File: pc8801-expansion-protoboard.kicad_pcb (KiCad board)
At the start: 2 copper layers, 219 x 95 mm, 4 parts, among them J1 Solder Side, J2 Parts Side

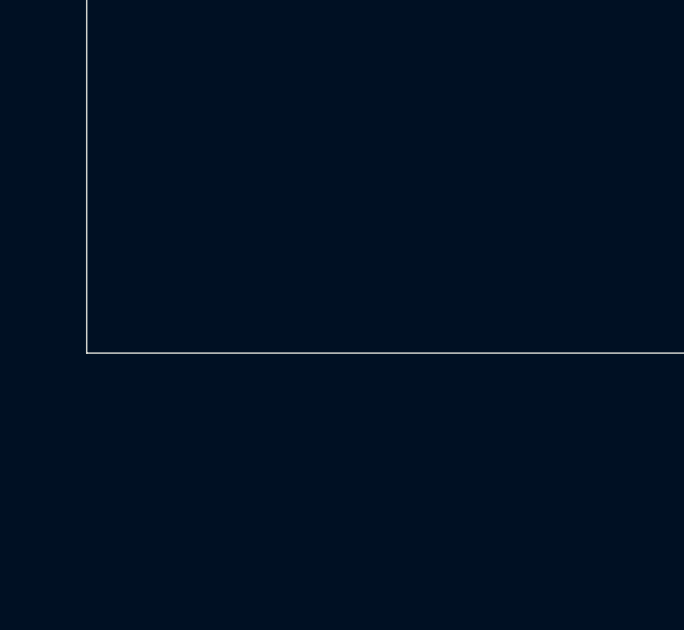
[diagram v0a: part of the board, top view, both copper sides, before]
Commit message: Minor silk prep
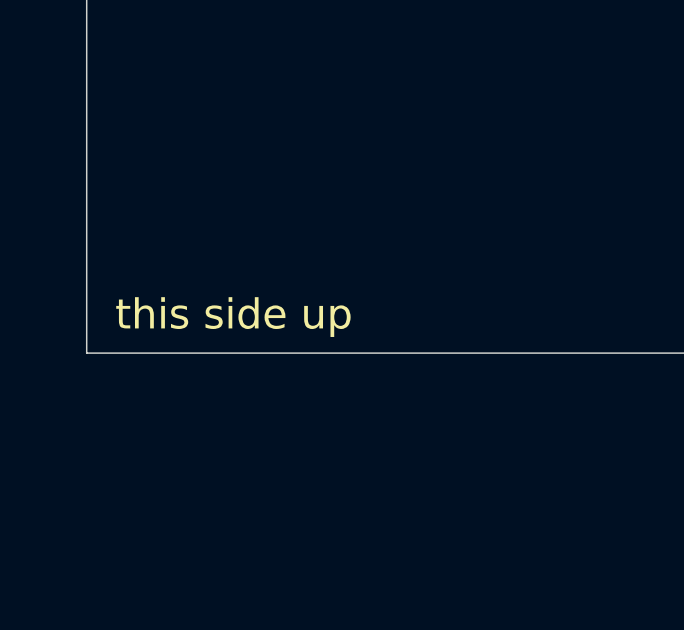
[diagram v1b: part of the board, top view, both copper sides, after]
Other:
- board text added: "this side up"
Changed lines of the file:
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@@
   (general
     (thickness 1.6)
-    (drawings 55)
+    (drawings 57)
     (tracks 7)
     (zones 0)
@@
   )
   (setup
-    (last_trace_width 2)
+    (last_trace_width 0.25)
     (user_trace_width 1)
     (user_trace_width 2)
@@
     (pad 1 np_thru_hole circle (at 0 0) (size 4.3 4.3) (drill 4.3) (layers *.Cu *.Mask))
   )
+  (gr_text "this side up" (at 41.91 132.715) (layer F.SilkS)
+    (effects (font (size 1 1) (thickness 0.15)))
+  )
+  (dimension 219 (width 0.12) (layer F.SilkS)
+    (gr_text "219.000 mm" (at 146.5 21.59) (layer F.SilkS)
+      (effects (font (size 1 1) (thickness 0.15)))
+    )
+    (feature1 (pts (xy 37 50) (xy 37 22.273579)))
+    (feature2 (pts (xy 256 50) (xy 256 22.273579)))
+    (crossbar (pts (xy 256 22.86) (xy 37 22.86)))
+    (arrow1a (pts (xy 37 22.86) (xy 38.126504 22.273579)))
+    (arrow1b (pts (xy 37 22.86) (xy 38.126504 23.446421)))
+    (arrow2a (pts (xy 256 22.86) (xy 254.873496 22.273579)))
+    (arrow2b (pts (xy 256 22.86) (xy 254.873496 23.446421)))
+  )
   (gr_text "AB\n0" (at 116.84 132.08) (layer F.SilkS)

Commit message: Power bars
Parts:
- added J3: 5V, PC-8801:1x20_PowerBar, F.Cu at (45.7, 66.0)
- added J4: 12V, PC-8801:1x20_PowerBar, F.Cu at (237.3, 66.0)
- added J5: -12V, PC-8801:1x20_PowerBar, F.Cu at (241.0, 66.0)
- added J6: GND_1, PC-8801:1x20_PowerBar, F.Cu at (49.5, 66.0)
- added J7: GND_2, PC-8801:1x20_PowerBar, F.Cu at (245.1, 66.0)
- added REF**: 70x20_ProtoArea, PC-8801:70x20_ProtoArea, F.Cu at (143.5, 90.2)
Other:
- board text added: "20 high"
- board text added: "70 wide"

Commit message: Power rails, of a sort
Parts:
- moved J3 3.81 mm to (49.5, 66.0)
- moved J6 3.81 mm to (45.7, 66.0)
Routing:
- net /GND: track 12.7 -> 386.8 mm
- net /+5V: track 15.2 -> 133.7 mm
- net /-12V: track 0.00 -> 103.7 mm
- net /+12V: track 0.00 -> 102.9 mm
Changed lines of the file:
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@@
     (thickness 1.6)
     (drawings 60)
-    (tracks 7)
+    (tracks 34)
     (zones 0)
     (modules 10)
@@
   )
   (setup
-    (last_trace_width 0.25)
+    (last_trace_width 2)
     (user_trace_width 1)
     (user_trace_width 2)
@@
   )
   (module PC-8801:1x20_PowerBar (layer F.Cu)
-    (at 49.53 66.04)
+    (at 45.72 66.04)
     (fp_text reference J6 (at 0 -2.54) (layer F.SilkS) hide
       (effects (font (size 1 1) (thickness 0.15)))
@@
   )
   (module PC-8801:1x20_PowerBar (layer F.Cu)
-    (at 45.72 66.04)
+    (at 49.53 66.04)
     (fp_text reference J3 (at 0 -2.54) (layer F.SilkS) hide
       (effects (font (size 1 1) (thickness 0.15)))
@@
   (segment (start 114.3 129.54) (end 114.3 124.46) (width 2) (layer F.Cu) (net 33))
   (segment (start 114.3 124.46) (end 111.76 124.46) (width 2) (layer F.Cu) (net 33))
+  (segment (start 111.76 124.46) (end 111.76 120.65) (width 2) (layer F.Cu) (net 33))
+  (segment (start 111.76 120.65) (end 110.49 119.38) (width 2) (layer F.Cu) (net 33))
+  (segment (start 110.49 119.38) (end 52.07 119.38) (width 2) (layer F.Cu) (net 33))
+  (segment (start 49.53 116.84) (end 49.53 66.04) (width 2) (layer F.Cu) (net 33))
+  (segment (start 52.07 119.38) (end 49.53 116.84) (width 2) (layer F.Cu) (net 33))
   (segment (start 109.22 124.46) (end 106.68 124.46) (width 2) (layer F.Cu) (net 34))
   (segment (start 106.68 124.46) (end 106.68 129.54) (width 2) (layer F.Cu) (net 34))
   (segment (start 109.22 129.54) (end 109.22 124.46) (width 2) (layer F.Cu) (net 34))
+  (segment (start 53.34 124.46) (end 109.22 124.46) (width 2) (layer F.Cu) (net 34))
+  (segment (start 45.72 116.84) (end 53.34 124.46) (width 2) (layer F.Cu) (net 34))
+  (segment (start 45.72 66.04) (end 45.72 116.84) (width 2) (layer F.Cu) (net 34))
+  (segment (start 45.72 66.04) (end 45.72 63.5) (width 2) (layer F.Cu) (net 34))
+  (segment (start 45.72 63.5) (end 49.53 59.69) (width 2) (layer F.Cu) (net 34))
+  (segment (start 49.53 59.69) (end 242.57 59.69) (width 2) (layer F.Cu) (net 34))
+  (segment (start 245.11 62.23) (end 245.11 114.3) (width 2) (layer F.Cu) (net 34))
+  (segment (start 242.57 59.69) (end 245.11 62.23) (width 2) (layer F.Cu) (net 34))
+  (segment (start 241 66.04) (end 241 114.3) (width 2) (layer F.Cu) (net 37))
+  (segment (start 234.441274 120.310008) (end 234.019992 120.310008) (width 2) (layer F.Cu) (net 37))
+  (segment (start 240.451283 114.3) (end 234.441274 120.310008) (width 2) (layer F.Cu) (net 37))
+  (segment (start 241 114.3) (end 240.451283 114.3) (width 2) (layer F.Cu) (net 37))
+  (segment (start 234.019992 120.310008) (end 233.68 120.65) (width 2) (layer F.Cu) (net 37))
+  (segment (start 233.68 120.65) (end 193.04 120.65) (width 2) (layer F.Cu) (net 37))
+  (segment (start 190.5 123.19) (end 190.5 124.46) (width 2) (layer F.Cu) (net 37))
+  (segment (start 193.04 120.65) (end 190.5 123.19) (width 2) (layer F.Cu) (net 37))
+  (segment (start 237.34 114.3) (end 237.34 66.04) (width 2) (layer F.Cu) (net 38))
+  (segment (start 236.578001 115.061999) (end 237.34 114.3) (width 2) (layer F.Cu) (net 38))
+  (segment (start 192.468715 118.11) (end 233.53 118.11) (width 2) (layer F.Cu) (net 38))
+  (segment (start 187.96 122.618715) (end 192.468715 118.11) (width 2) (layer F.Cu) (net 38))
+  (segment (start 187.96 124.46) (end 187.96 122.618715) (width 2) (layer F.Cu) (net 38))
+  (segment (start 233.53 118.11) (end 236.578001 115.061999) (width 2) (layer F.Cu) (net 38))
   (zone (net 34) (net_name /GND) (layer F.Cu) (hatch edge 0.508)
     (connect_pads yes (clearance 0.508))

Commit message: Here goes nothing
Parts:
- added U1: ExpansionEdge, PC-8801:PC88 Edge, F.Cu at (106.9, 138.7)
- moved J1 2.79 mm to (106.7, 126.7)
- moved J2 2.54 mm to (106.7, 121.9)
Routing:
- net /-12V: track 103.7 -> 166.3 mm
- net /+12V: track 102.9 -> 164.8 mm
- net /GND: track 386.8 -> 433.8 mm, vias 0 -> 4
- net /+5V: track 133.7 -> 177.4 mm, vias 0 -> 4
- net Net-(J2-Pad13): track 0.00 -> 18.0 mm
- net Net-(J2-Pad31): track 0.00 -> 17.8 mm
- net Net-(J2-Pad22): track 0.00 -> 17.8 mm
- net Net-(J2-Pad20): track 0.00 -> 17.8 mm
- net Net-(J2-Pad19): track 0.00 -> 17.8 mm
- net Net-(J2-Pad12): track 0.00 -> 17.8 mm
- net Net-(J2-Pad5): track 0.00 -> 17.8 mm
- net Net-(J2-Pad36): track 0.00 -> 17.8 mm, vias 0 -> 1
- net Net-(J2-Pad30): track 0.00 -> 17.8 mm
- net Net-(J2-Pad29): track 0.00 -> 17.8 mm
- net Net-(J2-Pad27): track 0.00 -> 17.8 mm
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- removed copper zone on F.Cu, net /+5V
- removed copper zone on F.Cu, net /GND

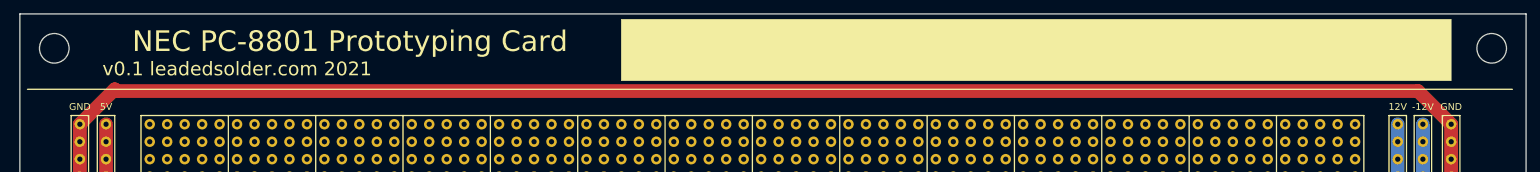
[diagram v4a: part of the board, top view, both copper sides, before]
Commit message: need to fix edge cut
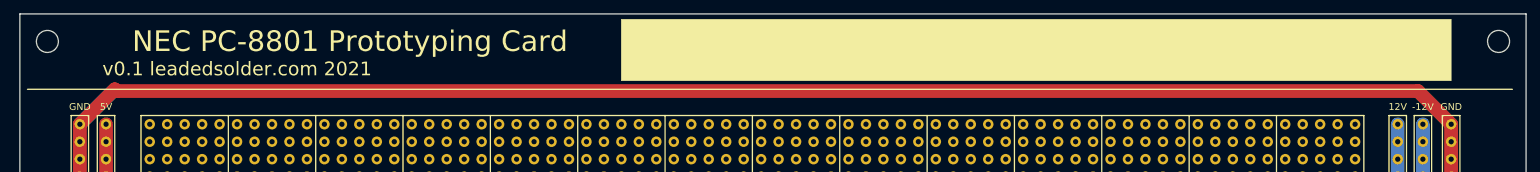
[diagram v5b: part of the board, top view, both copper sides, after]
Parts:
- removed the REF** at (42.0, 55.0)
- removed the REF** at (251.0, 55.0)
- added REF**: MountingHole_3.2mm_M3, MountingHole:MountingHole_3.2mm_M3, F.Cu at (41.0, 54.0)
- added REF**: MountingHole_3.2mm_M3, MountingHole:MountingHole_3.2mm_M3, F.Cu at (252.0, 54.0)
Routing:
- net /GND: track 433.8 -> 440.7 mm
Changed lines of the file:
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@@
   (general
     (thickness 1.6)
-    (drawings 60)
-    (tracks 295)
+    (drawings 64)
+    (tracks 296)
     (zones 0)
     (modules 11)
@@
   )
   (setup
-    (last_trace_width 0.25)
+    (last_trace_width 2)
     (user_trace_width 0.5)
     (user_trace_width 1)
@@
     (add_net "Net-(J2-Pad8)")
     (add_net "Net-(J2-Pad9)")
+  )
+  (module MountingHole:MountingHole_3.2mm_M3 locked (layer F.Cu)
+    (at 41 54)
+    (descr "Mounting Hole 3.2mm, no annular, M3")
+    (tags "mounting hole 3.2mm no annular m3")
+    (attr virtual)
+    (fp_text reference REF** (at 0 -4.2) (layer F.SilkS) hide
+      (effects (font (size 1 1) (thickness 0.15)))
+    )
+    (fp_text value MountingHole_3.2mm_M3 (at 0 4.2) (layer F.Fab)
+      (effects (font (size 1 1) (thickness 0.15)))
+    )
+    (fp_circle (center 0 0) (end 3.45 0) (layer F.CrtYd) (width 0.05))
+    (fp_circle (center 0 0) (end 3.2 0) (layer Cmts.User) (width 0.15))
+    (fp_text user %R (at 0.3 0) (layer F.Fab)
+      (effects (font (size 1 1) (thickness 0.15)))
+    )
+    (pad 1 np_thru_hole circle (at 0 0) (size 3.2 3.2) (drill 3.2) (layers *.Cu *.Mask))
+  )
+  (module MountingHole:MountingHole_3.2mm_M3 locked (layer F.Cu)
+    (at 252 54)
+    (descr "Mounting Hole 3.2mm, no annular, M3")
+    (tags "mounting hole 3.2mm no annular m3")
+    (attr virtual)
+    (fp_text reference REF** (at 0 -4.2) (layer F.SilkS) hide
+      (effects (font (size 1 1) (thickness 0.15)))
+    )
+    (fp_text value MountingHole_3.2mm_M3 (at 0 4.2) (layer F.Fab)
+      (effects (font (size 1 1) (thickness 0.15)))
+    )
+    (fp_circle (center 0 0) (end 3.45 0) (layer F.CrtYd) (width 0.05))
+    (fp_circle (center 0 0) (end 3.2 0) (layer Cmts.User) (width 0.15))
+    (fp_text user %R (at 0.3 0) (layer F.Fab)
+      (effects (font (size 1 1) (thickness 0.15)))
+    )
+    (pad 1 np_thru_hole circle (at 0 0) (size 3.2 3.2) (drill 3.2) (layers *.Cu *.Mask))
   )
   (module "PC-8801:PC88 Edge" (layer F.Cu)
@@
     )
   )
-  (module MountingHole:MountingHole_4.3mm_M4 locked (layer F.Cu)
-    (at 42 55)
-    (descr "Mounting Hole 4.3mm, no annular, M4")
-    (tags "mounting hole 4.3mm no annular m4")
-    (attr virtual)
-    (fp_text reference REF** (at 0 -5.3) (layer F.SilkS) hide
-      (effects (font (size 1 1) (thickness 0.15)))
-    )
-    (fp_text value MountingHole_4.3mm_M4 (at 0 5.3) (layer F.Fab)
-      (effects (font (size 1 1) (thickness 0.15)))
-    )
-    (fp_circle (center 0 0) (end 4.55 0) (layer F.CrtYd) (width 0.05))
-    (fp_circle (center 0 0) (end 4.3 0) (layer Cmts.User) (width 0.15))
-    (fp_text user %R (at 0.3 0) (layer F.Fab)
-      (effects (font (size 1 1) (thickness 0.15)))
-    )
-    (pad 1 np_thru_hole circle (at 0 0) (size 4.3 4.3) (drill 4.3) (layers *.Cu *.Mask))
-  )
-  (module MountingHole:MountingHole_4.3mm_M4 locked (layer F.Cu)
-    (at 251 55)
-    (descr "Mounting Hole 4.3mm, no annular, M4")
-    (tags "mounting hole 4.3mm no annular m4")
-    (attr virtual)
-    (fp_text reference REF** (at 0 -5.3) (layer F.SilkS) hide
-      (effects (font (size 1 1) (thickness 0.15)))
-    )
-    (fp_text value MountingHole_4.3mm_M4 (at 0 5.3) (layer F.Fab)
-      (effects (font (size 1 1) (thickness 0.15)))
-    )
-    (fp_circle (center 0 0) (end 4.55 0) (layer F.CrtYd) (width 0.05))
-    (fp_circle (center 0 0) (end 4.3 0) (layer Cmts.User) (width 0.15))
-    (fp_text user %R (at 0.3 0) (layer F.Fab)
-      (effects (font (size 1 1) (thickness 0.15)))
-    )
-    (pad 1 np_thru_hole circle (at 0 0) (size 4.3 4.3) (drill 4.3) (layers *.Cu *.Mask))
+  (dimension 7.5 (width 0.15) (layer Dwgs.User)
+    (gr_text "7.500 mm" (at 49.7 53.75 270) (layer Dwgs.User)
+      (effects (font (size 1 1) (thickness 0.15)))
+    )
+    (feature1 (pts (xy 37 57.5) (xy 48.986421 57.5)))
+    (feature2 (pts (xy 37 50) (xy 48.986421 50)))
+    (crossbar (pts (xy 48.4 50) (xy 48.4 57.5)))
+    (arrow1a (pts (xy 48.4 57.5) (xy 47.813579 56.373496)))
+    (arrow1b (pts (xy 48.4 57.5) (xy 48.986421 56.373496)))
+    (arrow2a (pts (xy 48.4 50) (xy 47.813579 51.126504)))
+    (arrow2b (pts (xy 48.4 50) (xy 48.986421 51.126504)))
+  )
+  (dimension 7.5 (width 0.15) (layer Dwgs.User)
+    (gr_text "7.500 mm" (at 40.75 62.8) (layer Dwgs.User)
+      (effects (font (size 1 1) (thickness 0.15)))
+    )
+    (feature1 (pts (xy 44.5 50) (xy 44.5 62.086421)))
+    (feature2 (pts (xy 37 50) (xy 37 62.086421)))
+    (crossbar (pts (xy 37 61.5) (xy 44.5 61.5)))
+    (arrow1a (pts (xy 44.5 61.5) (xy 43.373496 62.086421)))
+    (arrow1b (pts (xy 44.5 61.5) (xy 43.373496 60.913579)))
+    (arrow2a (pts (xy 37 61.5) (xy 38.126504 62.086421)))
+    (arrow2b (pts (xy 37 61.5) (xy 38.126504 60.913579)))
+  )
+  (dimension 7.5 (width 0.15) (layer Dwgs.User)
+    (gr_text "7.500 mm" (at 237.4 53.75 270) (layer Dwgs.User)
+      (effects (font (size 1 1) (thickness 0.15)))
+    )
+    (feature1 (pts (xy 256 57.5) (xy 238.113579 57.5)))
+    (feature2 (pts (xy 256 50) (xy 238.113579 50)))
+    (crossbar (pts (xy 238.7 50) (xy 238.7 57.5)))
+    (arrow1a (pts (xy 238.7 57.5) (xy 238.113579 56.373496)))
+    (arrow1b (pts (xy 238.7 57.5) (xy 239.286421 56.373496)))
+    (arrow2a (pts (xy 238.7 50) (xy 238.113579 51.126504)))
+    (arrow2b (pts (xy 238.7 50) (xy 239.286421 51.126504)))
+  )
+  (dimension 7.5 (width 0.15) (layer Dwgs.User)
+    (gr_text "7.500 mm" (at 252.25 40.5) (layer Dwgs.User)
+      (effects (font (size 1 1) (thickness 0.15)))
+    )
+    (feature1 (pts (xy 248.5 53.7) (xy 248.5 41.213579)))
+    (feature2 (pts (xy 256 53.7) (xy 256 41.213579)))
+    (crossbar (pts (xy 256 41.8) (xy 248.5 41.8)))
+    (arrow1a (pts (xy 248.5 41.8) (xy 249.626504 41.213579)))
+    (arrow1b (pts (xy 248.5 41.8) (xy 249.626504 42.386421)))
+    (arrow2a (pts (xy 256 41.8) (xy 254.873496 41.213579)))
+    (arrow2b (pts (xy 256 41.8) (xy 254.873496 42.386421)))
   )
   (gr_poly (pts (xy 245.11 59.69) (xy 124.46 59.69) (xy 124.46 50.8) (xy 245.11 50.8)) (layer F.SilkS) (width 0.1))
@@
   (segment (start 45.72 115.37763) (end 45.72 114.3) (width 2) (layer F.Cu) (net 34))
   (segment (start 45.72 66.04) (end 45.72 116.903285) (width 2) (layer F.Cu) (net 34))
+  (segment (start 245.11 66.04) (end 245.11 114.3) (width 2) (layer F.Cu) (net 34))
+  (segment (start 106.934 138.684) (end 106.934 132.08) (width 2) (layer B.Cu) (net 34))
+  (segment (start 45.72 66.04) (end 50.56 61.2) (width 2) (layer B.Cu) (net 34))
+  (segment (start 51.054 61.214) (end 240.284 61.214) (width 2) (layer F.Cu) (net 34))
+  (segment (start 240.284 61.214) (end 245.11 66.04) (width 2) (layer F.Cu) (net 34))
   (segment (start 45.72 66.04) (end 50.8 60.96) (width 2) (layer F.Cu) (net 34))
   (segment (start 50.8 60.96) (end 51.054 61.214) (width 2) (layer F.Cu) (net 34))
-  (segment (start 240.284 61.214) (end 245.11 66.04) (width 2) (layer F.Cu) (net 34))
-  (segment (start 51.054 61.214) (end 240.284 61.214) (width 2) (layer F.Cu) (net 34))
-  (segment (start 245.11 66.04) (end 245.11 114.3) (width 2) (layer F.Cu) (net 34))
-  (segment (start 106.934 138.684) (end 106.934 132.08) (width 2) (layer B.Cu) (net 34))
   (via (at 195.072 133.096) (size 0.8) (drill 0.4) (layers F.Cu B.Cu) (net 35))
   (segment (start 195.834 133.858) (end 195.072 133.096) (width 0.25) (layer B.Cu) (net 35))

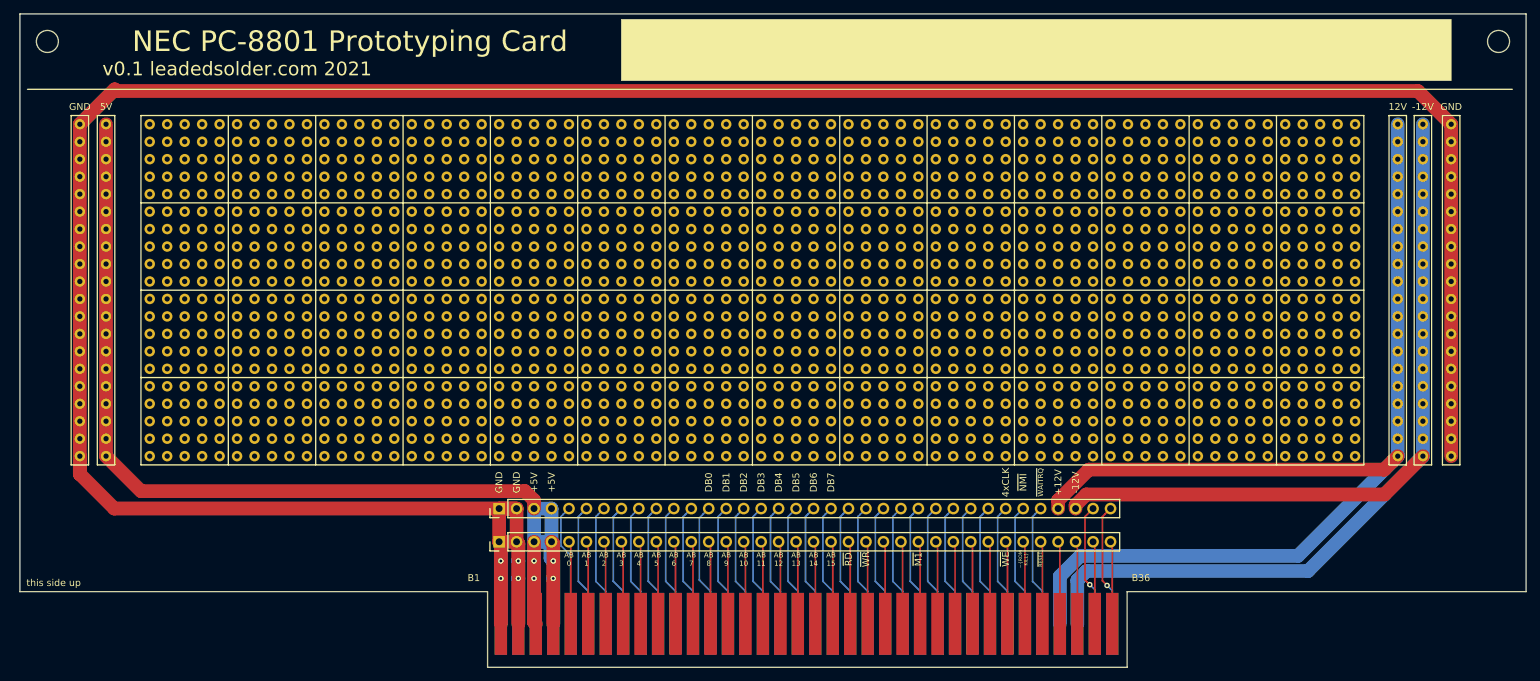
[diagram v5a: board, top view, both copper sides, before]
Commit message: Edge brought over to get closer to SB-II clone
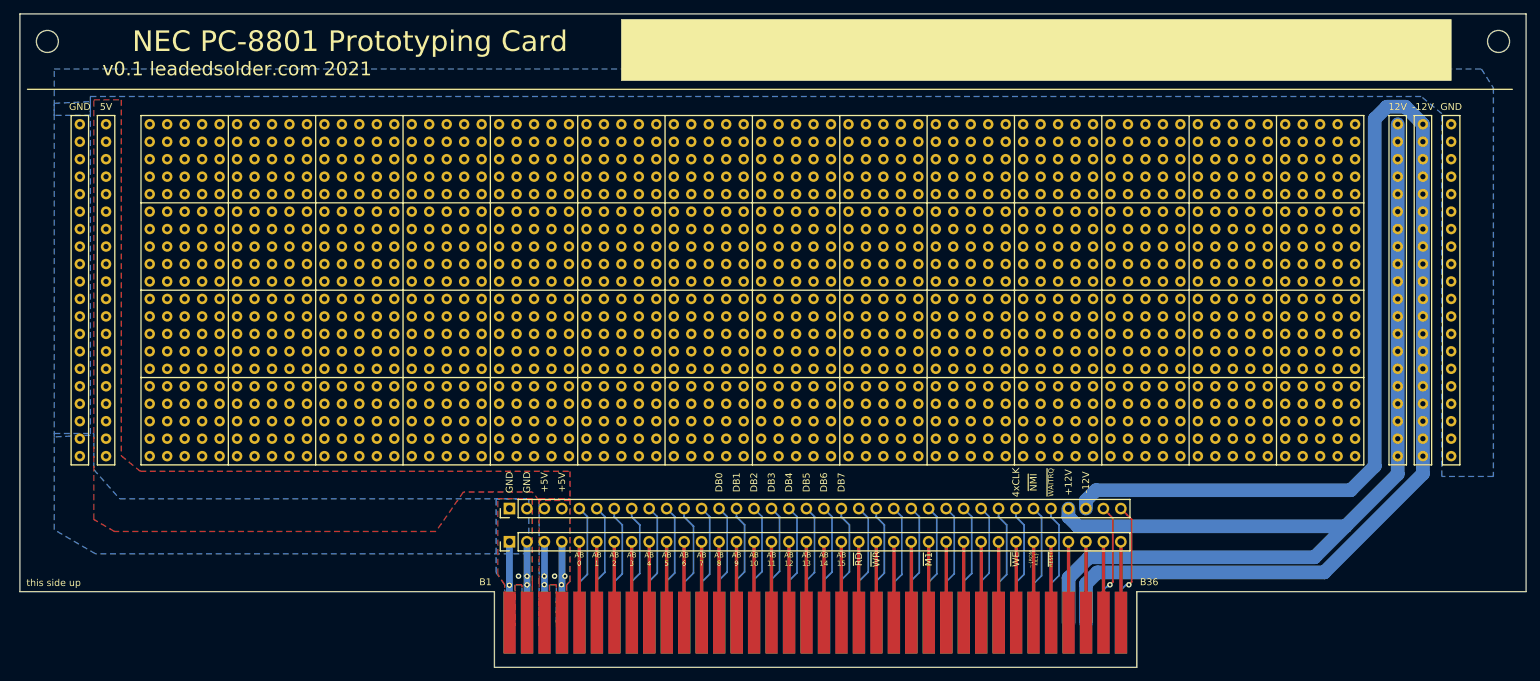
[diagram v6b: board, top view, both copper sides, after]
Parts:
- moved J1 1.50 mm to (108.2, 126.7)
- moved J2 1.50 mm to (108.2, 121.9)
- moved U1 1.28 mm to (108.2, 138.5)
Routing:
- net /GND: track 440.7 -> 23.5 mm
- net /+5V: track 177.4 -> 23.5 mm, vias 4 -> 5
- net /-12V: track 166.3 -> 216.6 mm
- net /+12V: track 164.8 -> 153.5 mm
- added copper zone on B.Cu, net /+5V
- added copper zone on F.Cu, net /+5V
- added copper zone on B.Cu, net /GND
- added copper zone on F.Cu, net /GND
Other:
- outline, holes or cut-outs redrawn
- board text added: "nice soldering, keep it up"
